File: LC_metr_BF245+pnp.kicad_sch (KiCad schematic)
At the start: 16 parts, among them J1 Conn_01x01_Socket, J2 Conn_01x01_Socket, J3 Conn_02x01, J4 Conn_01x01_Socket, J5 Conn_01x01_Socket, Q1 MPSA92, Q2 BF245A, U2 LM317_TO-252

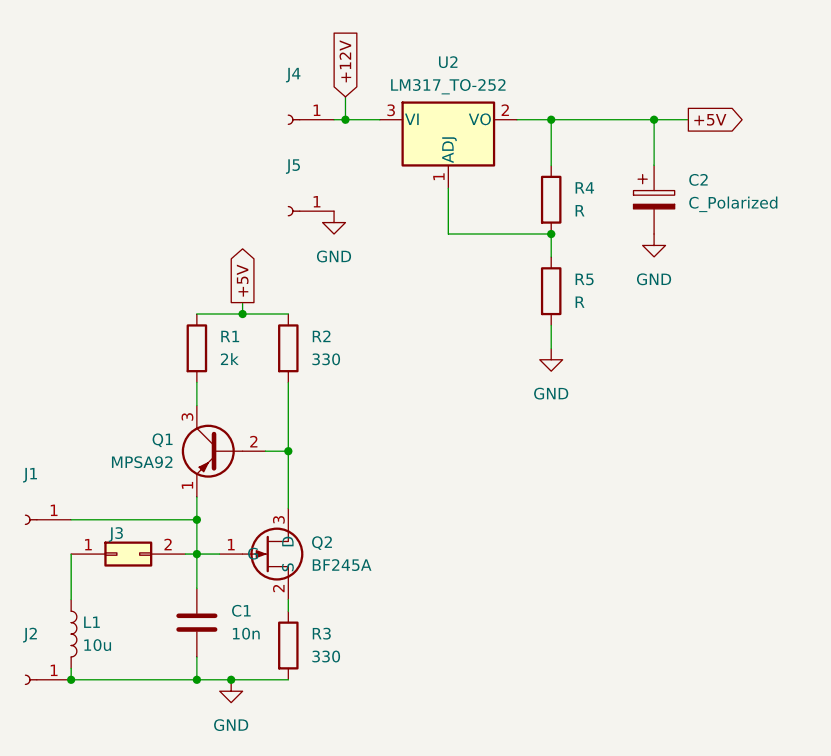
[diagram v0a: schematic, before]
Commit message: оптимизация и доработка
добавлены выходные клемы, оптимизированно размещение элементов топором
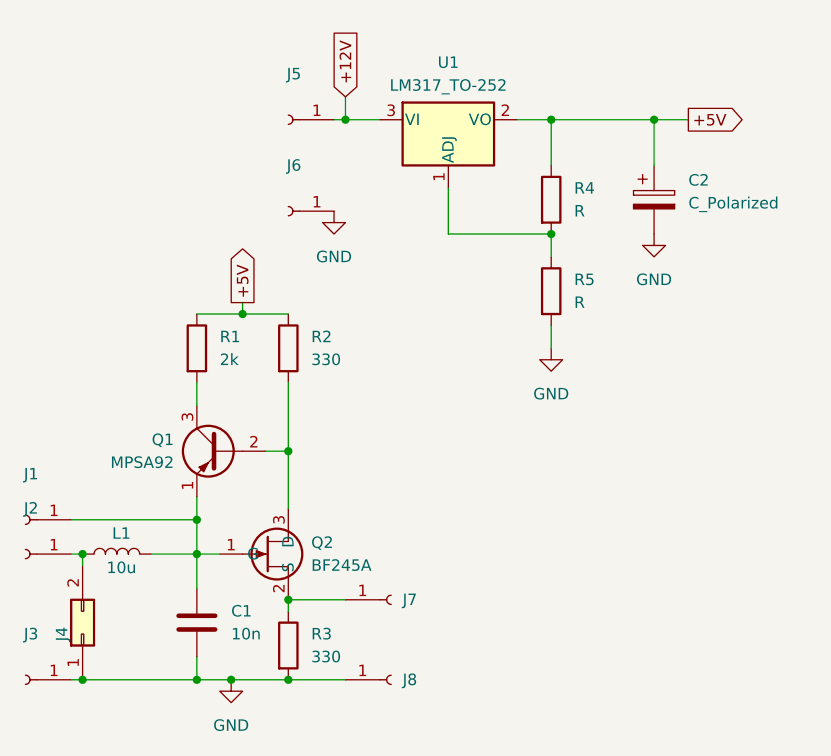
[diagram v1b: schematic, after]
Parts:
- added J2, J7, J8: Conn_01x01_Socket, main:Pin_3mm_Dril_1mm, symbol Connector:Conn_01x01_Socket
- renumbered J2 to J3, J3 to J4, J4 to J5, J5 to J6, U2 to U1
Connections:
- net GND: now also J4.1 (Pin_1), J8.1 (Pin_1); no longer L1.2
- net at C1.1, J1.1 (Pin_1), Q1.1 (E)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: now also L1.2; no longer J4.2 (Pin_2)
- net at Q2.2 (S), R3.1: now also J7.1 (Pin_1)
- net at L1.1: now also J4.2 (Pin_2), J2.1 (Pin_1); no longer J4.1 (Pin_1)
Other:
- moved on the sheet: J4, L1
